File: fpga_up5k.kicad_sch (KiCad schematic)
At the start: 52 parts, among them SW3 434121025816, SW4 434121025816, SW5 434121025816, U6 AP2112K-1.2, U7 ICE40UP5K-SG48ITR, X1 24MHz

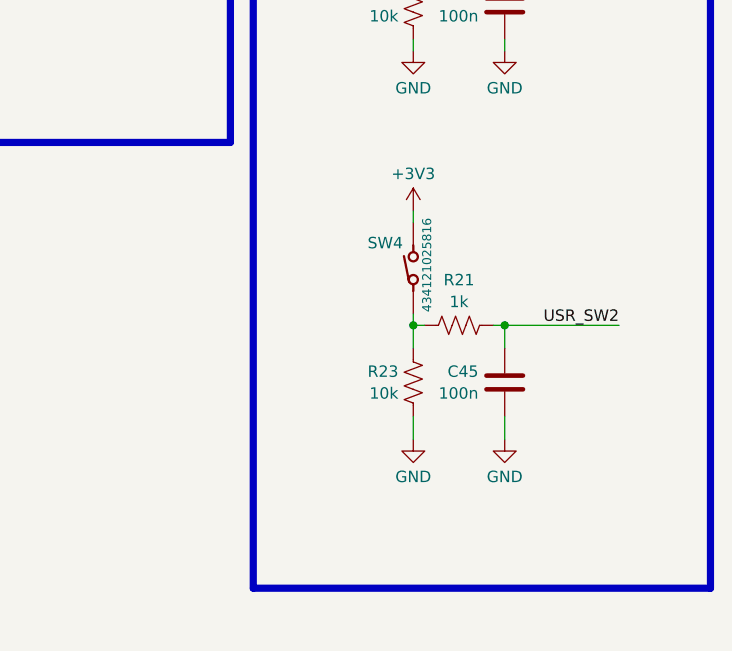
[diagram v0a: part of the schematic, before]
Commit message: revised to remove EF branding, adjust LED resistors, and invert SW2 button for reset.
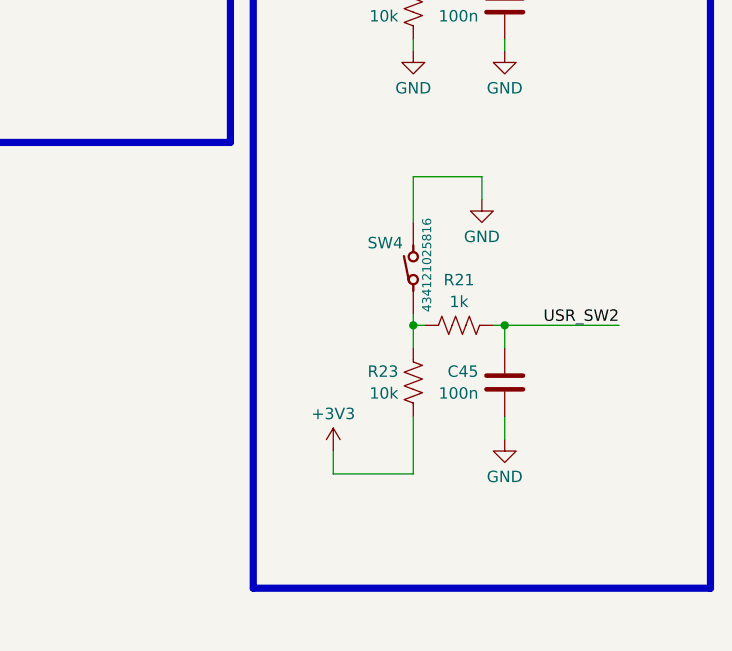
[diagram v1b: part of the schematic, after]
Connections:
- net +3V3: now also R23.2; no longer SW4.2
- net GND: now also SW4.2; no longer R23.2
